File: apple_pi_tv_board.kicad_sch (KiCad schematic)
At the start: 7 parts, among them J1 RJ45, U1 HDMI/USB, U2 apple tv tos link

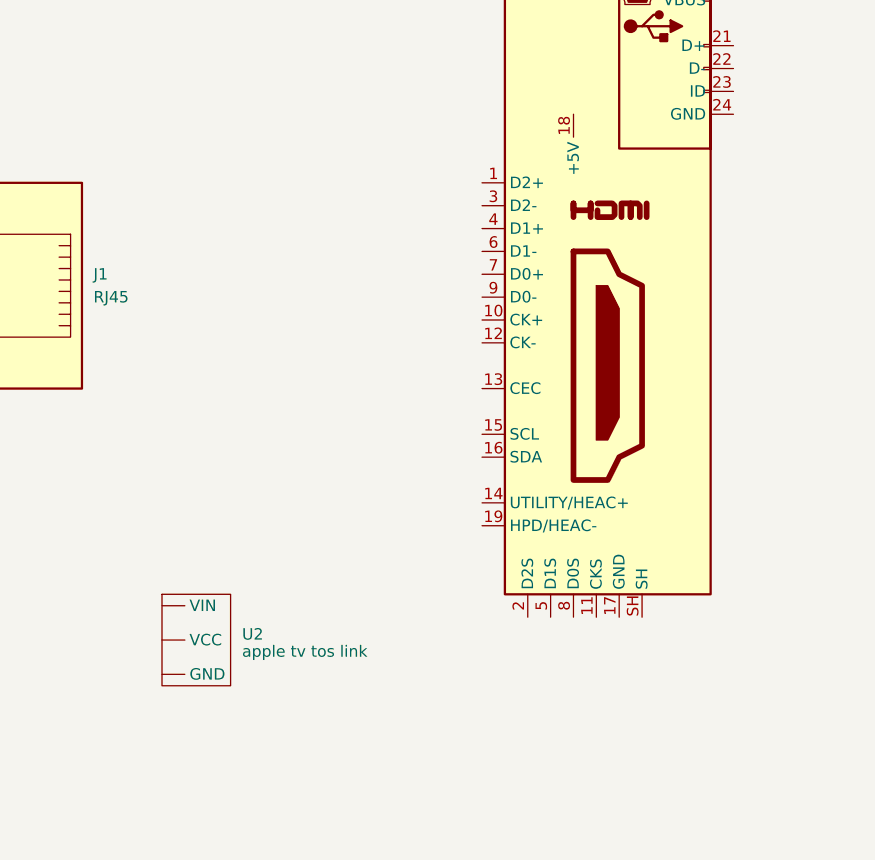
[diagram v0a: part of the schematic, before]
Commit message: moved the parts slightly
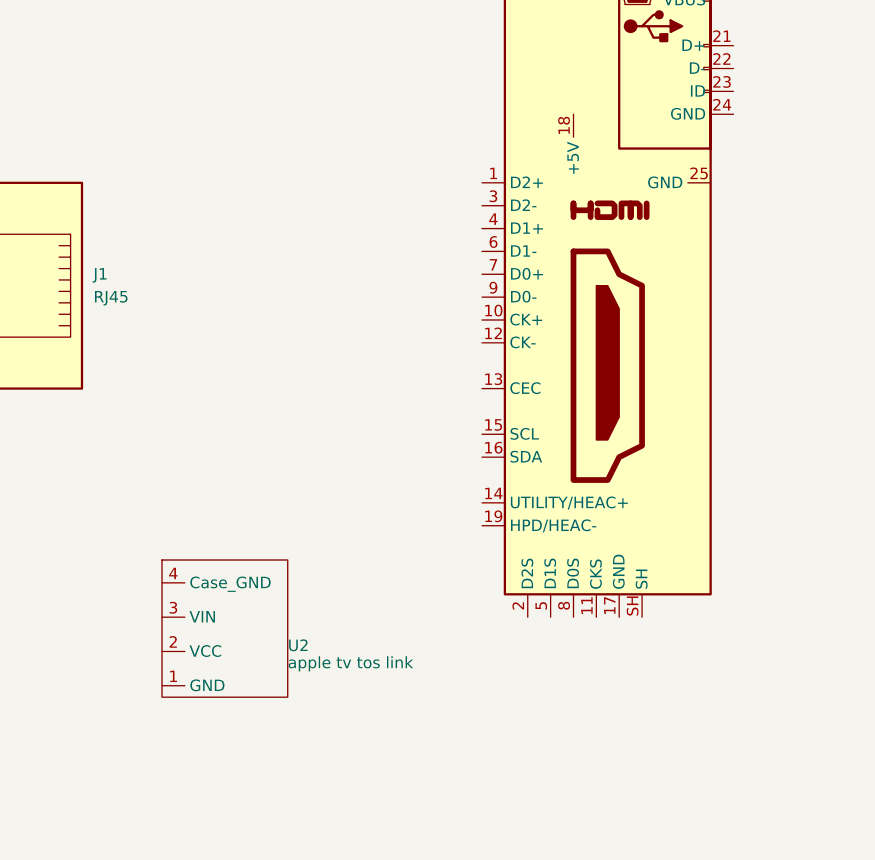
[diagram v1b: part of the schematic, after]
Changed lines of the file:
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@@
 		(pin "3"
+		)
+		(pin "25"
 		)
 		(instances
@@
 	(symbol
 		(lib_id "apple_tv_parts:apple_tv_tos_link")
-		(at 140.97 97.79 0)
+		(at 146.05 99.06 0)
 		(unit 1)
 		(exclude_from_sim no)
@@
 		(fields_autoplaced yes)
 		(property "Reference" "U2"
-			(at 147.32 100.9649 0)
+			(at 152.4 102.2349 0)
 			(effects
 				(font
@@
 		)
 		(property "Value" "apple tv tos link"
-			(at 147.32 102.87 0)
+			(at 152.4 104.14 0)
 			(effects
 				(font
@@
 		)
 		(property "Footprint" "apple_tv_parts:apple_tv_tos_link"
-			(at 140.97 97.79 0)
+			(at 146.05 99.06 0)
 			(effects
 				(font
@@
 		)
 		(property "Datasheet" ""
-			(at 140.97 97.79 0)
+			(at 146.05 99.06 0)
 			(effects
 				(font
@@
 		)
 		(property "Description" ""
-			(at 140.97 97.79 0)
+			(at 146.05 99.06 0)
 			(effects
 				(font
@@
 			)
 		)
-		(pin ""
+		(pin "3"
 		)
-		(pin ""
+		(pin "1"
 		)
-		(pin ""
+		(pin "2"
+		)
+		(pin "4"
 		)
 		(instances
-			(project ""
+			(project "apple_pi_tv_board"
 				(path "/391fcf0b-b604-4ad0-921e-8f3dad9a49eb"
 					(reference "U2")
